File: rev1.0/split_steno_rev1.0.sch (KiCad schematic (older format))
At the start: 45 parts, among them J0 Audio-Jack-4, K0 KEYSW, K1 KEYSW, K10 KEYSW, K11 KEYSW, K12 KEYSW, K13 KEYSW, K14 KEYSW, K15 KEYSW, K16 KEYSW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

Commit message: reorganized schematic library and pro micro footprint
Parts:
- removed C0: CP, Capacitors_THT:CP_Radial_D4.0mm_P2.00mm, symbol CP
- removed R0: 500, Keebio-Parts:Resistor-Hybrid, symbol R
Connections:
- net raw is gone; now on net VCC: U0.~ (VCC)
- net d2: no longer names the net of U0.4 (A6)
- net miso: no longer names the net of U0.14 (MISO)
- net mosi: no longer names the net of U0.16 (MOSI)
- net pwm: no longer names the net of U0.10 (A10/PWM)
- net rx: no longer names the net of U0.0 (RX)
- net sclk: no longer names the net of U0.15 (SCLK)
- net tx: no longer names the net of U0.1 (TX)
- no-connect marks 0 -> 8
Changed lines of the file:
@@
 EESchema Schematic File Version 2
+LIBS:split_steno_rev1.0
 LIBS:keyboard_parts
 LIBS:ws2812b
@@
 LIBS:contrib
 LIBS:valves
-LIBS:split_steno_rev1.0-cache
 EELAYER 25 0
 EELAYER END
@@
 Text Label 7050 1550 2    60   ~ 0
 d1
-Text Label 7850 3000 1    60   ~ 0
-d2
-$Comp
-L R R0
-U 1 1 5A98D003
-P 7850 3250
-F 0 "R0" V 7930 3250 50  0000 C CNN
-F 1 "500" V 7850 3250 50  0000 C CNN
-F 2 "Keebio-Parts:Resistor-Hybrid" H 7850 3250 60  0001 C CNN
-F 3 "" H 7850 3250 60  0000 C CNN
-	1    7850 3250
-	-1   0    0    1
-$EndComp
-Text Label 7050 1650 2    60   ~ 0
-d2
 Wire Wire Line
 	3250 1950 3250 1850
@@
 Connection ~ 5250 2950
 Connection ~ 5250 4000
-$Comp
-L CP C0
-U 1 1 5AA06AA7
-P 7200 3200
-F 0 "C0" H 7225 3300 50  0000 L CNN
-F 1 "CP" H 7225 3100 50  0000 L CNN
-F 2 "Capacitors_THT:CP_Radial_D4.0mm_P2.00mm" H 7238 3050 50  0001 C CNN
-F 3 "" H 7200 3200 50  0001 C CNN
-	1    7200 3200
-	1    0    0    -1
-$EndComp
-$Comp
-L VCC #PWR07
-U 1 1 5AA06BB0
-P 7200 3050
-F 0 "#PWR07" H 7200 2900 50  0001 C CNN
-F 1 "VCC" H 7200 3200 50  0000 C CNN
-F 2 "" H 7200 3050 50  0001 C CNN
-F 3 "" H 7200 3050 50  0001 C CNN
-	1    7200 3050
-	1    0    0    -1
-$EndComp
-$Comp
-L GND #PWR08
-U 1 1 5AA06C4D
-P 7200 3350
-F 0 "#PWR08" H 7200 3100 50  0001 C CNN
-F 1 "GND" H 7200 3200 50  0000 C CNN
-F 2 "" H 7200 3350 50  0001 C CNN
-F 3 "" H 7200 3350 50  0001 C CNN
-	1    7200 3350
-	1    0    0    -1
-$EndComp
-Text Label 7850 3500 0    60   ~ 0
-dout
-Text Label 8450 1050 0    60   ~ 0
-raw
-Text Label 8450 1850 0    60   ~ 0
-sclk
-Text Label 8450 1950 0    60   ~ 0
-miso
-Text Label 8450 2050 0    60   ~ 0
-mosi
-Text Label 8450 2150 0    60   ~ 0
-pwm
-Text Label 7050 1050 2    60   ~ 0
-tx
-Text Label 7050 1150 2    60   ~ 0
-rx
 Wire Wire Line
 	7050 1350 7050 1250
@@
 	1    0    0    -1
 $EndComp
+NoConn ~ 8450 1950
+NoConn ~ 8450 2050
+NoConn ~ 8450 2150
+NoConn ~ 8450 1050
+NoConn ~ 7050 1050
+NoConn ~ 7050 1150
+NoConn ~ 7050 1650
+NoConn ~ 8450 1850
 $EndSCHEMATC

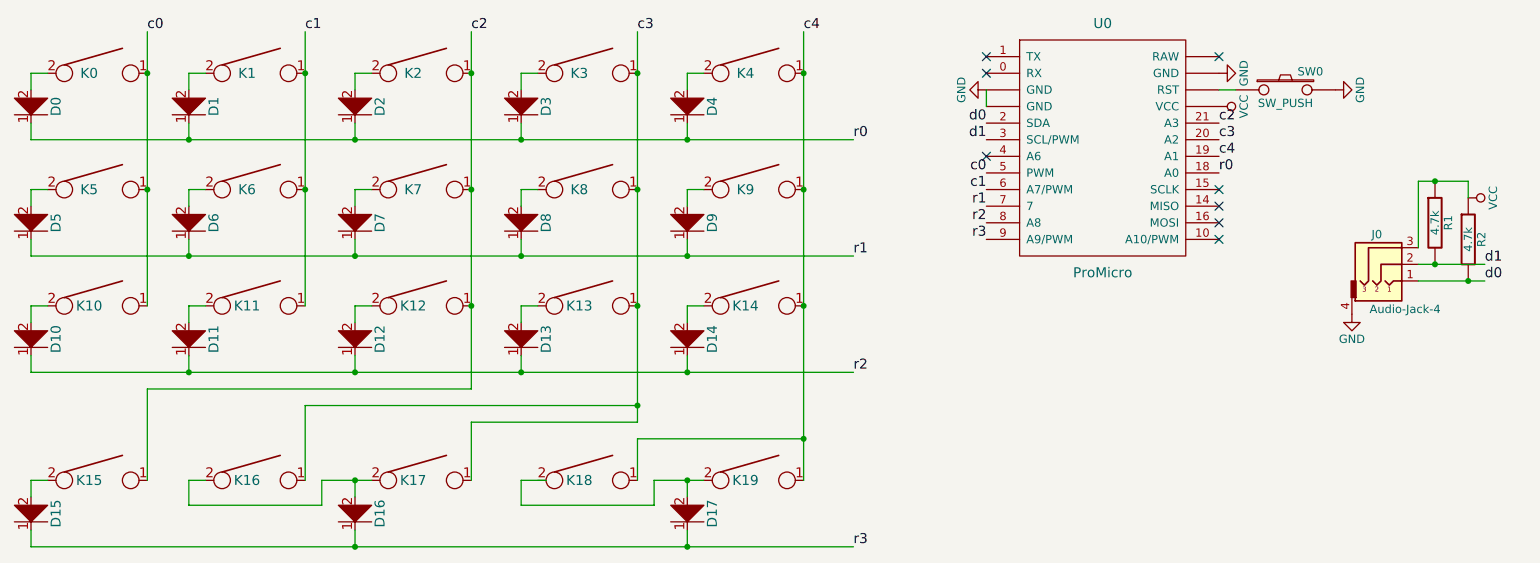
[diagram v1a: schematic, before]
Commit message: removed global libraries and moved to local versions
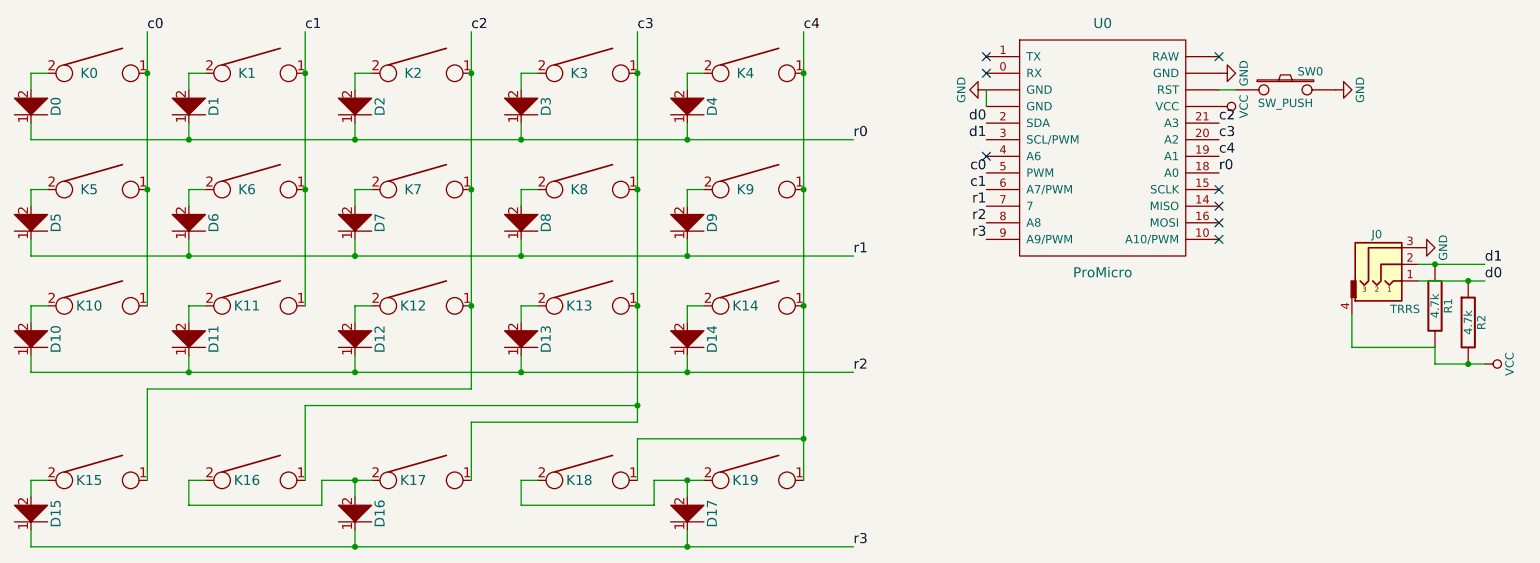
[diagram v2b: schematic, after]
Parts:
- D0, D1, D10, D11, D12, D13, D14, D15, D16, D17, D2, D3, D4, D5, D6, D7, D8, D9: footprint Keebio-Parts:Diode-dual -> lib_fp:Diode-dual
- J0: value Audio-Jack-4 -> TRRS; footprint Keebio-Parts:TRRS-PJ-320A -> lib_fp:TRRS-PJ-320A
- K0, K1, K10, K11, K12, K13, K14, K15, K17, K19, K2, K3, K4, K5, K6, K7, K8, K9: footprint Keebio-Parts:Hybrid_PCB_100H_Dual_hole -> lib_fp:Hybrid_PCB_100H_Dual_hole
- K16, K18: footprint Keebio-Parts:Hybrid_PCB_200H-dual-nosilk -> lib_fp:Hybrid_PCB_200H-dual-nosilk
- R1, R2: footprint Keebio-Parts:Resistor-Hybrid -> lib_fp:Resistor-Hybrid
- SW0: footprint Keebio-Parts:SW_Tactile_SPST_Angled_MJTP1117 -> lib_fp:SW_Tactile_SPST_Angled_MJTP1117
- U0: footprint Keebio-Parts:ArduinoProMicro -> lib_fp:ArduinoProMicro
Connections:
- net GND: now also J0.3; no longer J0.4
- net VCC: now also J0.4, R1.2, R2.2; no longer J0.3, R1.1, R2.1
- net d0: now also R2.1; no longer R2.2
- net d1: now also R1.1; no longer R1.2
- net at K18.2: now also D17.2, K19.2
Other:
- moved on the sheet: R1, R2

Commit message: finished routing traces
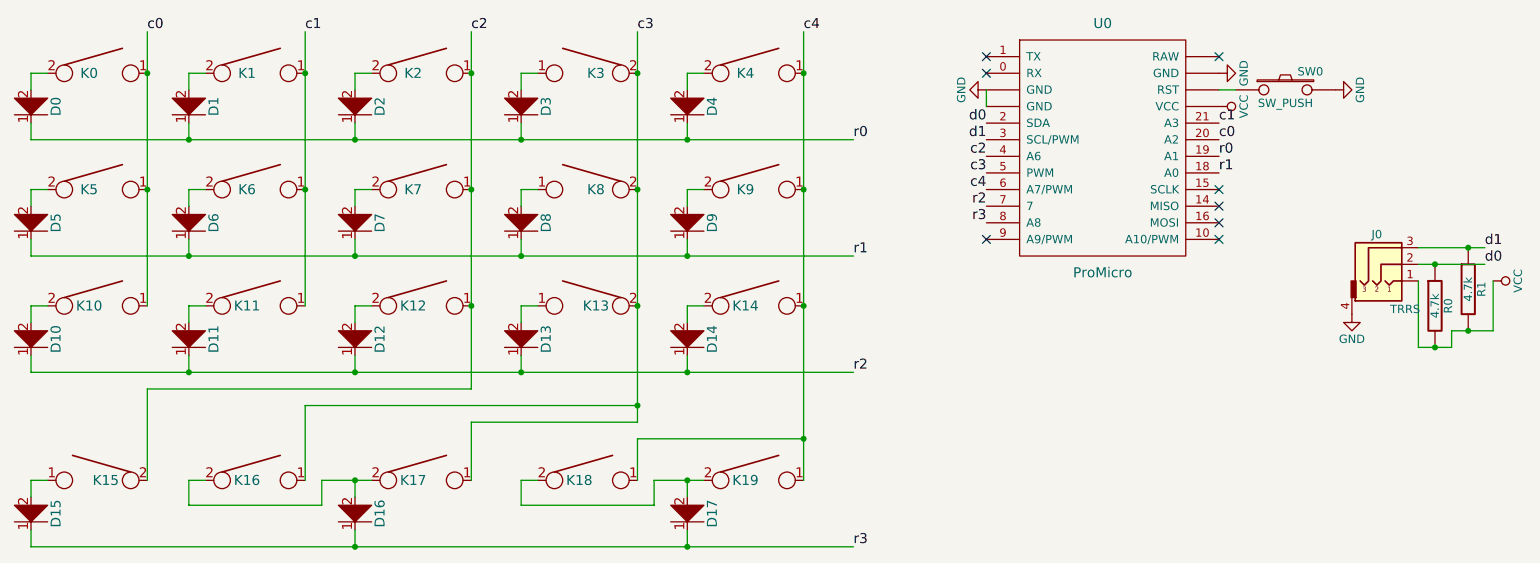
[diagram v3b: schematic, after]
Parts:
- renumbered R1 to R0, R2 to R1
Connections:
- net GND: now also J0.4; no longer J0.3
- net VCC: now also J0.1; no longer J0.4
- net c0: now also U0.20 (A2); no longer U0.5 (PWM)
- net c1: now also U0.21 (A3); no longer U0.6 (A7/PWM)
- net c2: now also K15.2, U0.4 (A6); no longer K15.1, U0.21 (A3)
- net c3: now also K13.2, K3.2, K8.2, U0.5 (PWM); no longer K13.1, K3.1, K8.1, U0.20 (A2)
- net c4: now also U0.6 (A7/PWM); no longer U0.19 (A1)
- net d0: now also J0.2, R0.1; no longer J0.1, R1.1
- net d1: now also J0.3, R1.1; no longer J0.2, R0.1
- net r0: now also U0.19 (A1); no longer U0.18 (A0)
- net r1: now also U0.18 (A0); no longer U0.7
- net r2: now also U0.7; no longer U0.8 (A8)
- net r3: now also U0.8 (A8); no longer U0.9 (A9/PWM)
- net at D8.2: now also K8.1; no longer K8.2
- net at D13.2: now also K13.1; no longer K13.2
- net at D3.2: now also K3.1; no longer K3.2
- net at D15.2: now also K15.1; no longer K15.2
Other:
- moved on the sheet: R1
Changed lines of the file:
@@
 Date "2018-02-28"
 Rev "1.0"
-Comp ""
+Comp "jtallbean"
 Comment1 ""
 Comment2 ""
@@
 F 3 "" H 4650 1850 60  0000 C CNN
 	1    4650 1850
-	1    0    0    -1
+	-1   0    0    -1
 $EndComp
 $Comp
@@
 F 3 "" H 4650 2550 60  0000 C CNN
 	1    4650 2550
-	1    0    0    -1
+	-1   0    0    -1
 $EndComp
 $Comp
@@
 F 3 "" H 4650 1150 60  0000 C CNN
 	1    4650 1150
-	1    0    0    -1
+	-1   0    0    -1
 $EndComp
 $Comp
@@
 F 3 "" H 1700 3600 60  0000 C CNN
 	1    1700 3600
-	1    0    0    -1
+	-1   0    0    -1
 $EndComp
 $Comp
@@
 Text Label 5950 900  0    60   ~ 0
 c4
+Text Label 8450 1550 0    60   ~ 0
+c0
+Text Label 7050 1650 2    60   ~ 0
+c2
 Text Label 7050 1750 2    60   ~ 0
-c0
+c3
+Text Label 7050 1850 2    60   ~ 0
+c4
+Text Label 8450 1650 0    60   ~ 0
+r0
+Text Label 8450 1750 0    60   ~ 0
+r1
+Text Label 7050 1950 2    60   ~ 0
+r2
+Text Label 7050 2050 2    60   ~ 0
+r3
 Text Label 8450 1450 0    60   ~ 0
-c2
-Text Label 8450 1550 0    60   ~ 0
-c3
-Text Label 8450 1650 0    60   ~ 0
-c4
-Text Label 8450 1750 0    60   ~ 0
-r0
-Text Label 7050 1950 2    60   ~ 0
-r1
-Text Label 7050 2050 2    60   ~ 0
-r2
-Text Label 7050 2150 2    60   ~ 0
-r3
-Text Label 7050 1850 2    60   ~ 0
 c1
 $Comp
@@
 L GND #PWR05
 U 1 1 5A98E990
-P 9650 2200
-F 0 "#PWR05" H 9650 1950 50  0001 C CNN
-F 1 "GND" H 9650 2050 50  0000 C CNN
-F 2 "" H 9650 2200 50  0001 C CNN
-F 3 "" H 9650 2200 50  0001 C CNN
-	1    9650 2200
-	0    -1   -1   0
+P 9250 2600
+F 0 "#PWR05" H 9250 2350 50  0001 C CNN
+F 1 "GND" H 9250 2450 50  0000 C CNN
+F 2 "" H 9250 2600 50  0001 C CNN
+F 3 "" H 9250 2600 50  0001 C CNN
+	1    9250 2600
+	1    0    0    -1
 $EndComp
 $Comp
 L VCC #PWR06
 U 1 1 5A98EC7D
-P 10050 2900
-F 0 "#PWR06" H 10050 2750 50  0001 C CNN
-F 1 "VCC" H 10050 3050 50  0000 C CNN
-F 2 "" H 10050 2900 50  0001 C CNN
-F 3 "" H 10050 2900 50  0001 C CNN
-	1    10050 2900
+P 10100 2400
+F 0 "#PWR06" H 10100 2250 50  0001 C CNN
+F 1 "VCC" H 10100 2550 50  0000 C CNN
+F 2 "" H 10100 2400 50  0001 C CNN
+F 3 "" H 10100 2400 50  0001 C CNN
+	1    10100 2400
 	0    1    1    0
 $EndComp
 $Comp
-L R R2
-U 1 1 5A98F1B9
-P 9950 2650
-F 0 "R2" V 10030 2650 50  0000 C CNN
-F 1 "4.7k" V 9950 2650 50  0000 C CNN
-F 2 "lib_fp:Resistor-Hybrid" H 9950 2650 60  0001 C CNN
-F 3 "" H 9950 2650 60  0000 C CNN
-	1    9950 2650
-	1    0    0    -1
-$EndComp
-$Comp
-L R R1
+L R R0
 U 1 1 5A98F2A4
 P 9750 2550
-F 0 "R1" V 9830 2550 50  0000 C CNN
+F 0 "R0" V 9830 2550 50  0000 C CNN
 F 1 "4.7k" V 9750 2550 50  0000 C CNN
 F 2 "lib_fp:Resistor-Hybrid" H 9750 2550 60  0001 C CNN
@@
 	1    0    0    -1
 $EndComp
-Text Label 10050 2400 0    60   ~ 0
+Text Label 10050 2300 0    60   ~ 0
 d0
-Text Label 10050 2300 0    60   ~ 0
+Text Label 10050 2200 0    60   ~ 0
 d1
 Text Label 7050 1450 2    60   ~ 0
@@
 NoConn ~ 8450 1950
 NoConn ~ 8450 2050
-NoConn ~ 8450 2150
 NoConn ~ 8450 1050
 NoConn ~ 7050 1050
 NoConn ~ 7050 1150
-NoConn ~ 7050 1650
 NoConn ~ 8450 1850
+$Comp
+L R R1
+U 1 1 5A98F1B9
+P 9950 2450
+F 0 "R1" V 10030 2450 50  0000 C CNN
+F 1 "4.7k" V 9950 2450 50  0000 C CNN
+F 2 "lib_fp:Resistor-Hybrid" H 9950 2450 60  0001 C CNN
+F 3 "" H 9950 2450 60  0000 C CNN
+	1    9950 2450
+	1    0    0    -1
+$EndComp
 Wire Wire Line
 	3250 1950 3250 1850
@@
 	7050 1350 7050 1250
 Wire Wire Line
+	8450 1250 8550 1250
+Wire Wire Line
+	4250 3600 4350 3600
+Wire Wire Line
 	9650 2300 10050 2300
-Wire Wire Line
-	9650 2400 10050 2400
 Connection ~ 9750 2300
-Connection ~ 9950 2400
-Wire Wire Line
-	8450 1250 8550 1250
-Wire Wire Line
-	4250 3600 4350 3600
-Wire Wire Line
-	9250 2600 9250 2800
-Wire Wire Line
-	9250 2800 9750 2800
-Wire Wire Line
-	9750 2800 9750 2900
-Wire Wire Line
-	9750 2900 10050 2900
-Connection ~ 9950 2900
+Wire Wire Line
+	9650 2200 10050 2200
+Connection ~ 9950 2200
+Wire Wire Line
+	9650 2400 9650 2800
+Wire Wire Line
+	9650 2800 9850 2800
+Wire Wire Line
+	9850 2800 9850 2700
+Wire Wire Line
+	9850 2700 10100 2700
+Connection ~ 9750 2800
+Wire Wire Line
+	10100 2700 10100 2400
+Connection ~ 9950 2700
+NoConn ~ 8450 2150
+NoConn ~ 7050 2150
 $EndSCHEMATC
